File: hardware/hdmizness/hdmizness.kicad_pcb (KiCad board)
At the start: 2 copper layers, 85.6 x 54 mm, 65 parts, among them J1 HDMI_A_PCB, J2 USB_A_PCB, SW1 SW_Push, U1 F1C100s, U2 TDA19988, U3 W25Q128JVPIQ, U4 EA3058, Y1 24M

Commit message: pcb: Add front design
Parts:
- added Ref**: Val**, hdmizness:card_front, F.Cu at (124.6, 78.1)
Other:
- board text added: "A"
- board text added: "Ba"
- board text added: "le"
- board text added: "n"
- board text added: "u"
- board text added: "v1.0 - (c) 2020"
- board text added: "vi"
- board text added: "xis"

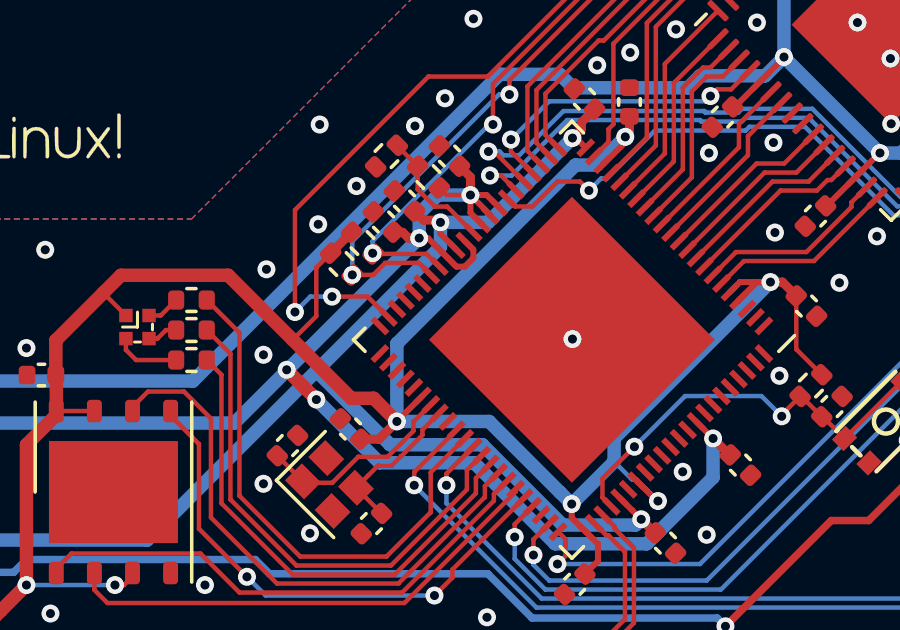
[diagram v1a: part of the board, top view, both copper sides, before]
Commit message: hdmizness: Add board revision hard straps
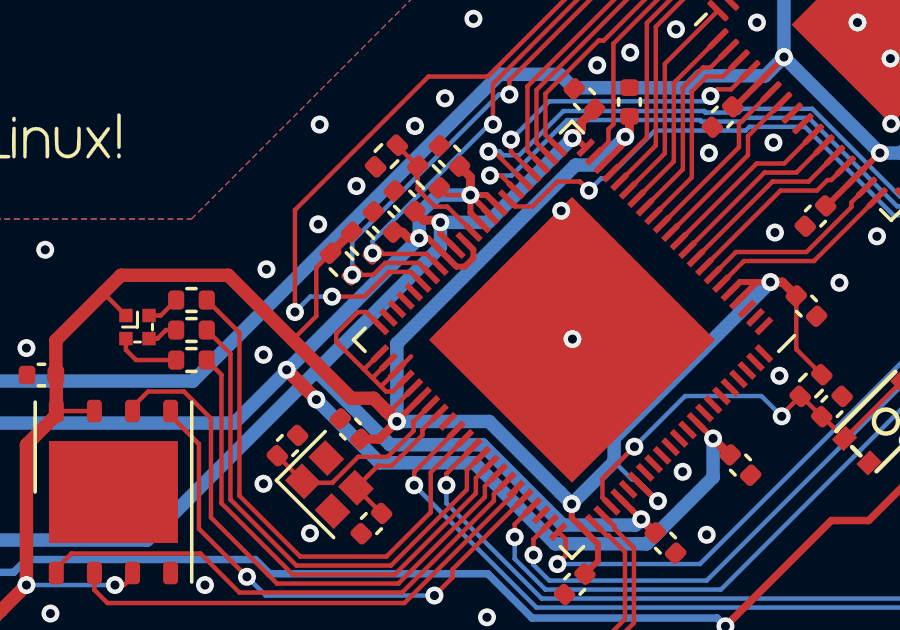
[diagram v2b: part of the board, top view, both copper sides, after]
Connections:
- U1 pad 39: Net-(U1-Pad39) -> /HDMI_INT
- U1 pad 43: /HDMI_INT -> Net-(U1-Pad43)
- U1 pad 44: Net-(U1-Pad44) -> GND
- U1 pad 45: Net-(U1-Pad45) -> GND
- U1 pad 46: Net-(U1-Pad46) -> GND
- U1 pad 47: Net-(U1-Pad47) -> GND
- U1 pad 48: Net-(U1-Pad48) -> GND
- U1 pad 49: Net-(U1-Pad49) -> +3V3
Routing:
- net GND: track 33.8 -> 42.2 mm, vias 79 -> 80
- net /HDMI_INT: track 31.6 -> 32.9 mm
- net +3V3: track 103.4 -> 104.6 mm
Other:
- board text added: "Board version hard straps are not all directly connected to the GND underneath the CPU for easier bodging, if the need arises."
